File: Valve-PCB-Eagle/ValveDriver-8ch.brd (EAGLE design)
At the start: 101.6 x 63.5 mm, 21 parts, among them IC1 ULQ2803A, J10 Valve 3, J11 Valve 2, J12 Valve 1, J4 POWER_JACK, J5 Valve 8, J6 Valve 7, J7 Valve 6, J8 Valve 5, J9 Valve 4

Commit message: [Valve][Teensy] Fix mistaken labeling of Lick1/Lick2 pins
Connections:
- net LICK_1: now also J14.2, U$1.8; no longer J14.3, U$1.7
- net LICK_2: now also J14.3, U$1.7; no longer J14.2, U$1.8
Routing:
- net LICK_2: track 73.5 -> 84.7 mm
- net LICK_1: track 84.7 -> 73.5 mm
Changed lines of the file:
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@@
 <wire x1="56.53" y1="52.07" x2="29.21" y2="52.07" width="0.3048" layer="1"/>
 </signal>
-<signal name="LICK_1">
+<signal name="LICK_2">
 <contactref element="U$1" pad="7"/>
 <contactref element="J14" pad="3"/>
@@
 <wire x1="29.21" y1="26.67" x2="95.25" y2="26.67" width="0.3048" layer="1"/>
 </signal>
-<signal name="LICK_2">
+<signal name="LICK_1">
 <contactref element="U$1" pad="8"/>
 <contactref element="J14" pad="2"/>

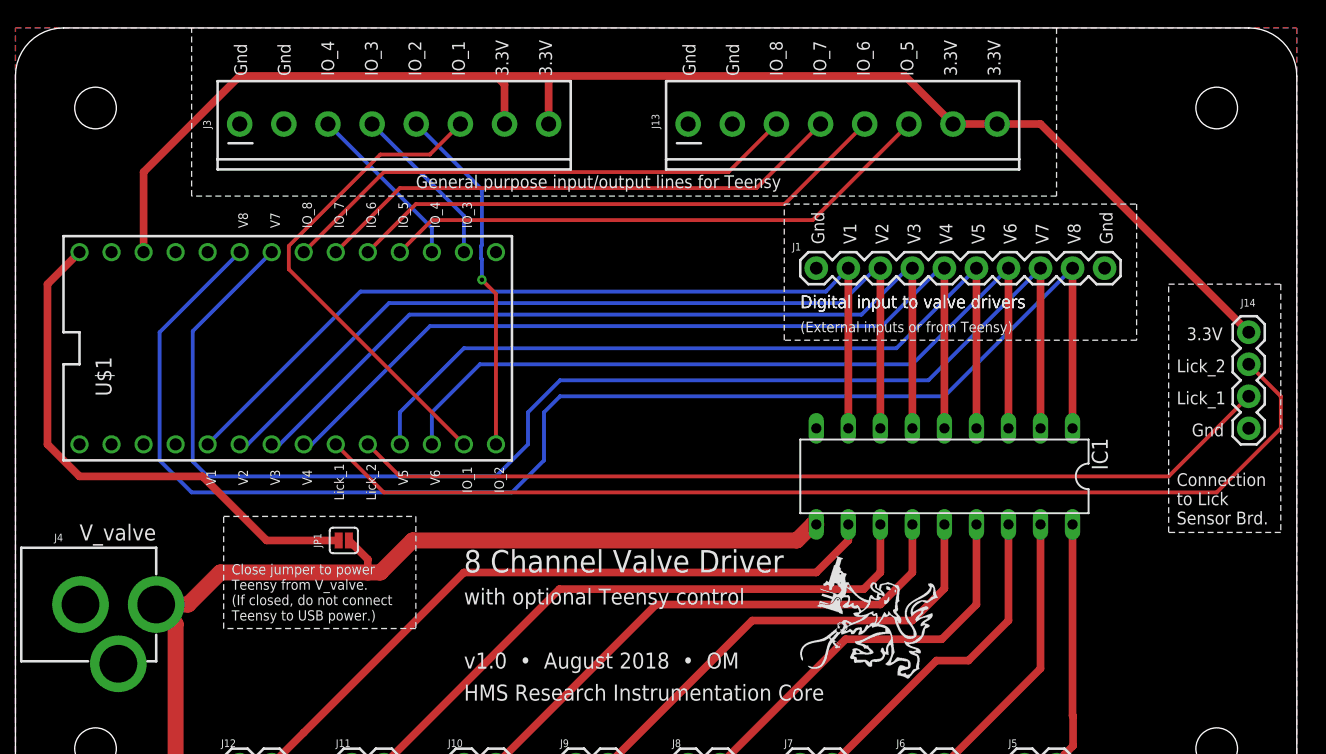
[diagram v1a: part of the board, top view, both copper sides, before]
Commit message: [Valve] Add 5V to screw term (fixes #6)
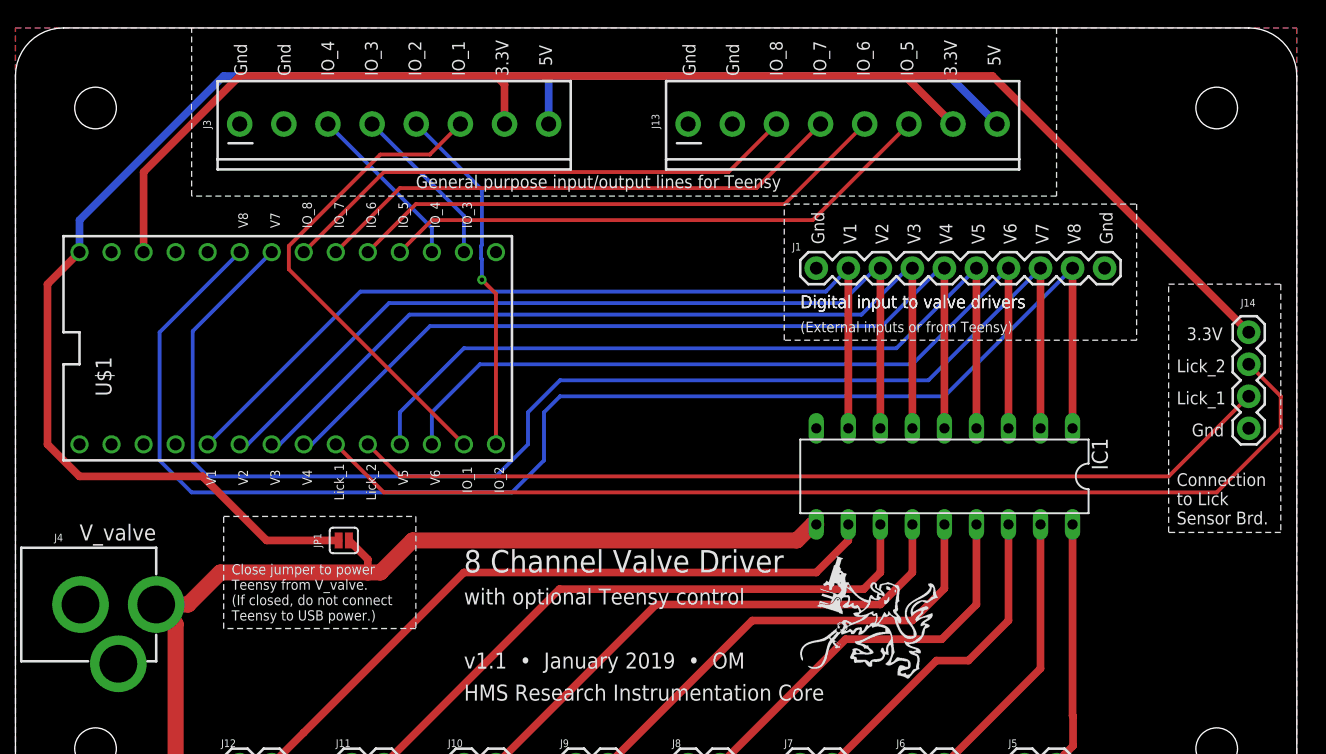
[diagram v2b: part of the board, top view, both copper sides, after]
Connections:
- net 3.3V: no longer J13.8, J3.8
- net V_IN_TEENSY: now also J13.8, J3.8
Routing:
- net V_IN_TEENSY: track 42.5 -> 128.1 mm
- net 3.3V: track 113.6 -> 115.0 mm
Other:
- board text added: "Gnd Gnd IO_4 IO_3 IO_2 IO_1 3.3V 5V"
- board text added: "Gnd Gnd IO_8 IO_7 IO_6 IO_5 3.3V 5V"
- board text added: "v1.1 • January 2019 • OM"
- board text removed: "Gnd Gnd IO_4 IO_3 IO_2 IO_1 3.3V 3.3V"
- board text removed: "Gnd Gnd IO_8 IO_7 IO_6 IO_5 3.3V 3.3V"
- board text removed: "v1.0 • August 2018 • OM"
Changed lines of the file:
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@@
 <?xml version="1.0" encoding="utf-8"?>
 <!DOCTYPE eagle SYSTEM "eagle.dtd">
-<eagle version="9.1.1">
+<eagle version="9.2.2">
 <drawing>
 <settings>
@@
 <setting verticaltext="up"/>
 </settings>
-<grid distance="0.1" unitdist="inch" unit="inch" style="dots" multiple="1" display="yes" altdistance="0.025" altunitdist="inch" altunit="inch"/>
+<grid distance="0.05" unitdist="inch" unit="inch" style="lines" multiple="2" display="yes" altdistance="0.025" altunitdist="inch" altunit="inch"/>
 <layers>
 <layer number="1" name="Top" color="4" fill="1" visible="yes" active="yes"/>
@@
 <layer number="18" name="Vias" color="2" fill="1" visible="yes" active="yes"/>
 <layer number="19" name="Unrouted" color="6" fill="1" visible="yes" active="yes"/>
-<layer number="20" name="Dimension" color="24" fill="1" visible="yes" active="yes"/>
-<layer number="21" name="tPlace" color="7" fill="1" visible="yes" active="yes"/>
-<layer number="22" name="bPlace" color="7" fill="1" visible="yes" active="yes"/>
-<layer number="23" name="tOrigins" color="15" fill="1" visible="no" active="yes"/>
-<layer number="24" name="bOrigins" color="15" fill="1" visible="no" active="yes"/>
-<layer number="25" name="tNames" color="7" fill="1" visible="yes" active="yes"/>
-<layer number="26" name="bNames" color="7" fill="1" visible="yes" active="yes"/>
-<layer number="27" name="tValues" color="7" fill="1" visible="yes" active="yes"/>
-<layer number="28" name="bValues" color="7" fill="1" visible="yes" active="yes"/>
+<layer number="20" name="Dimension" color="15" fill="1" visible="yes" active="yes"/>
+<layer number="21" name="tPlace" color="15" fill="1" visible="yes" active="yes"/>
+<layer number="22" name="bPlace" color="14" fill="1" visible="yes" active="yes"/>
+<layer number="23" name="tOrigins" color="15" fill="1" visible="yes" active="yes"/>
+<layer number="24" name="bOrigins" color="15" fill="1" visible="yes" active="yes"/>
+<layer number="25" name="tNames" color="15" fill="1" visible="no" active="yes"/>
+<layer number="26" name="bNames" color="15" fill="1" visible="no" active="yes"/>
+<layer number="27" name="tValues" color="7" fill="1" visible="no" active="yes"/>
+<layer number="28" name="bValues" color="7" fill="1" visible="no" active="yes"/>
 <layer number="29" name="tStop" color="7" fill="3" visible="no" active="yes"/>
 <layer number="30" name="bStop" color="7" fill="6" visible="no" active="yes"/>
@@
 <layer number="37" name="tTest" color="7" fill="1" visible="no" active="yes"/>
 <layer number="38" name="bTest" color="7" fill="1" visible="no" active="yes"/>
-<layer number="39" name="tKeepout" color="4" fill="11" visible="yes" active="yes"/>
-<layer number="40" name="bKeepout" color="1" fill="11" visible="yes" active="yes"/>
-<layer number="41" name="tRestrict" color="4" fill="10" visible="yes" active="yes"/>
-<layer number="42" name="bRestrict" color="1" fill="10" visible="yes" active="yes"/>
+<layer number="39" name="tKeepout" color="4" fill="11" visible="no" active="yes"/>
+<layer number="40" name="bKeepout" color="1" fill="11" visible="no" active="yes"/>
+<layer number="41" name="tRestrict" color="4" fill="10" visible="no" active="yes"/>
+<layer number="42" name="bRestrict" color="1" fill="10" visible="no" active="yes"/>
 <layer number="43" name="vRestrict" color="2" fill="10" visible="no" active="yes"/>
 <layer number="44" name="Drills" color="7" fill="1" visible="no" active="yes"/>
-<layer number="45" name="Holes" color="7" fill="1" visible="no" active="yes"/>
+<layer number="45" name="Holes" color="7" fill="1" visible="yes" active="yes"/>
 <layer number="46" name="Milling" color="3" fill="1" visible="no" active="yes"/>
 <layer number="47" name="Measures" color="7" fill="1" visible="no" active="yes"/>
@@
 <layer number="49" name="Reference" color="7" fill="1" visible="no" active="yes"/>
 <layer number="50" name="dxf" color="7" fill="1" visible="no" active="no"/>
-<layer number="51" name="tDocu" color="7" fill="1" visible="yes" active="yes"/>
-<layer number="52" name="bDocu" color="7" fill="1" visible="yes" active="yes"/>
+<layer number="51" name="tDocu" color="6" fill="1" visible="yes" active="yes"/>
+<layer number="52" name="bDocu" color="7" fill="1" visible="no" active="yes"/>
 <layer number="53" name="tGND_GNDA" color="7" fill="9" visible="no" active="no"/>
 <layer number="54" name="bGND_GNDA" color="1" fill="9" visible="no" active="no"/>
@@
 <text x="35.56" y="20.32" size="1.778" layer="21" ratio="15">8 Channel Valve Driver</text>
 <text x="35.56" y="17.78" size="1.27" layer="21" ratio="15">with optional Teensy control</text>
-<text x="35.56" y="12.7" size="1.27" layer="21" ratio="10">v1.0  •  August 2018  •  OM</text>
+<text x="35.56" y="12.7" size="1.27" layer="21" ratio="10">v1.1  •  January 2019  •  OM</text>
 <text x="35.56" y="10.16" size="1.27" layer="21" ratio="10">HMS Research Instrumentation Core</text>
 <text x="17.145" y="16.51" size="0.8128" layer="21" ratio="12">Close jumper to power
@@
 IO_1
 3.3V
-3.3V</text>
+  5V</text>
 <text x="78.105" y="59.69" size="1.016" layer="21" ratio="15" distance="240" rot="R90">Gnd
 Gnd
@@
 IO_5
 3.3V
-3.3V</text>
+  5V</text>
 <text x="31.75" y="50.8" size="1.016" layer="21">General purpose input/output lines for Teensy</text>
 <wire x1="13.97" y1="50.165" x2="13.97" y2="63.5" width="0.0762" layer="21" style="shortdash"/>
@@
 </autorouter>
 <elements>
-<element name="IC1" library="uln-udn" library_urn="urn:adsk.eagle:library:407" package="DIL18" package3d_urn="urn:adsk.eagle:package:30237/1" value="ULQ2803A" x="73.66" y="27.94" rot="R180"/>
+<element name="IC1" library="uln-udn" library_urn="urn:adsk.eagle:library:407" package="DIL18" package3d_urn="urn:adsk.eagle:package:30237/1" value="ULQ2803A" x="73.66" y="27.94" smashed="yes" rot="R180">
+<attribute name="NAME" x="85.344" y="30.988" size="1.27" layer="25" ratio="10" rot="R270"/>
+<attribute name="VALUE" x="83.185" y="28.575" size="1.27" layer="27" ratio="10" rot="R180"/>
+</element>
 <element name="J1" library="SparkFun-Connectors" package="1X10" value="" x="63.5" y="44.45" smashed="yes">
 <attribute name="NAME" x="61.595" y="45.847" size="0.6096" layer="25" font="vector" ratio="15"/>
@@
 <attribute name="NAME" x="24.257" y="22.86" size="0.6096" layer="25" font="vector" ratio="15" rot="R90" align="bottom-center"/>
 </element>
-<element name="U$3" library="ofer-eagle-lib" package="RIC_LOGO_MED" value="" x="62.23" y="11.8872"/>
+<element name="U$3" library="ofer-eagle-lib" package="RIC_LOGO_MED" value="" x="62.23" y="11.8872" smashed="yes"/>
 <element name="U$2" library="SparkFun-Hardware" library_urn="urn:adsk.eagle:library:519" package="STAND-OFF" package3d_urn="urn:adsk.eagle:package:38630/1" value="" x="95.25" y="57.15" smashed="yes">
 <attribute name="VALUE" x="95.25" y="55.118" size="0.6096" layer="27" font="vector" ratio="20" align="top-center"/>
@@
 <wire x1="10.16" y1="52.07" x2="17.78" y2="59.69" width="0.6096" layer="1"/>
 <wire x1="17.78" y1="59.69" x2="38.1" y2="59.69" width="0.6096" layer="1"/>
-<wire x1="38.1" y1="59.69" x2="41.91" y2="59.69" width="0.6096" layer="1"/>
-<wire x1="41.91" y1="59.69" x2="70.53" y2="59.69" width="0.6096" layer="1"/>
+<wire x1="38.1" y1="59.69" x2="70.53" y2="59.69" width="0.6096" layer="1"/>
 <wire x1="70.53" y1="59.69" x2="74.34" y2="55.88" width="0.6096" layer="1"/>
 <wire x1="38.78" y1="55.88" x2="38.78" y2="59.01" width="0.6096" layer="1"/>
 <wire x1="38.78" y1="59.01" x2="38.1" y2="59.69" width="0.6096" layer="1"/>
-<contactref element="J13" pad="8"/>
-<contactref element="J3" pad="8"/>
 <contactref element="J14" pad="4"/>
-<wire x1="42.28" y1="55.88" x2="42.28" y2="59.32" width="0.6096" layer="1"/>
-<wire x1="42.28" y1="59.32" x2="41.91" y2="59.69" width="0.6096" layer="1"/>
-<wire x1="74.34" y1="55.88" x2="77.84" y2="55.88" width="0.6096" layer="1"/>
-<wire x1="77.84" y1="55.88" x2="81.28" y2="55.88" width="0.6096" layer="1"/>
-<wire x1="81.28" y1="55.88" x2="97.79" y2="39.37" width="0.6096" layer="1"/>
+<wire x1="70.53" y1="59.69" x2="77.47" y2="59.69" width="0.6096" layer="1"/>
+<wire x1="77.47" y1="59.69" x2="97.79" y2="39.37" width="0.6096" layer="1"/>
 </signal>
 <signal name="GND" class="1">
@@
 <wire x1="19.9136" y1="22.86" x2="25.6286" y2="22.86" width="0.6096" layer="1"/>
 <wire x1="5.08" y1="27.94" x2="14.8336" y2="27.94" width="0.6096" layer="1"/>
+<contactref element="J3" pad="8"/>
+<contactref element="J13" pad="8"/>
+<wire x1="5.08" y1="45.72" x2="5.08" y2="48.26" width="0.6096" layer="16"/>
+<wire x1="5.08" y1="48.26" x2="16.51" y2="59.69" width="0.6096" layer="16"/>
+<wire x1="16.51" y1="59.69" x2="41.91" y2="59.69" width="0.6096" layer="16"/>
+<wire x1="41.91" y1="59.69" x2="42.28" y2="59.32" width="0.6096" layer="16"/>
+<wire x1="42.28" y1="59.32" x2="42.28" y2="55.88" width="0.6096" layer="16"/>
+<wire x1="41.91" y1="59.69" x2="74.03" y2="59.69" width="0.6096" layer="16"/>
+<wire x1="74.03" y1="59.69" x2="77.84" y2="55.88" width="0.6096" layer="16"/>
 </signal>
 </signals>

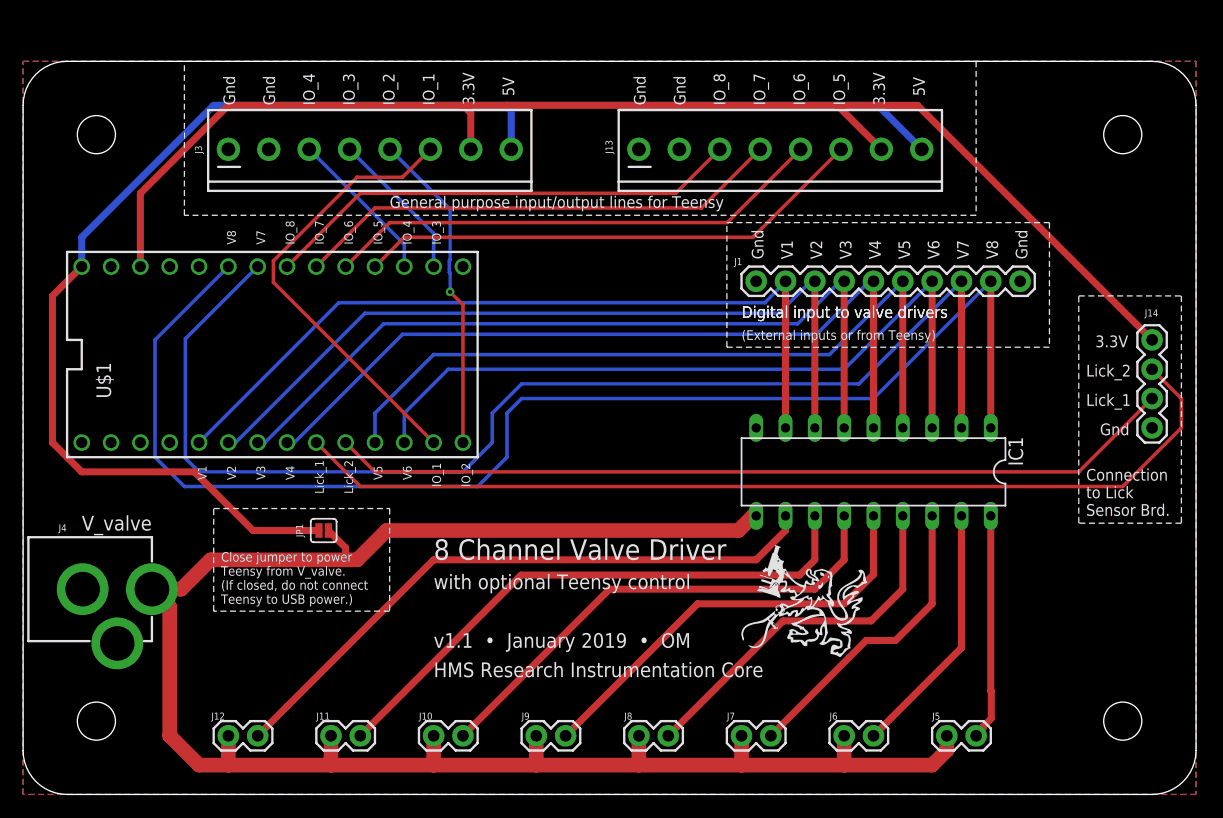
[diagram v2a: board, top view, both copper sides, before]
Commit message: [Valve] Make minor tweaks to board size & layout
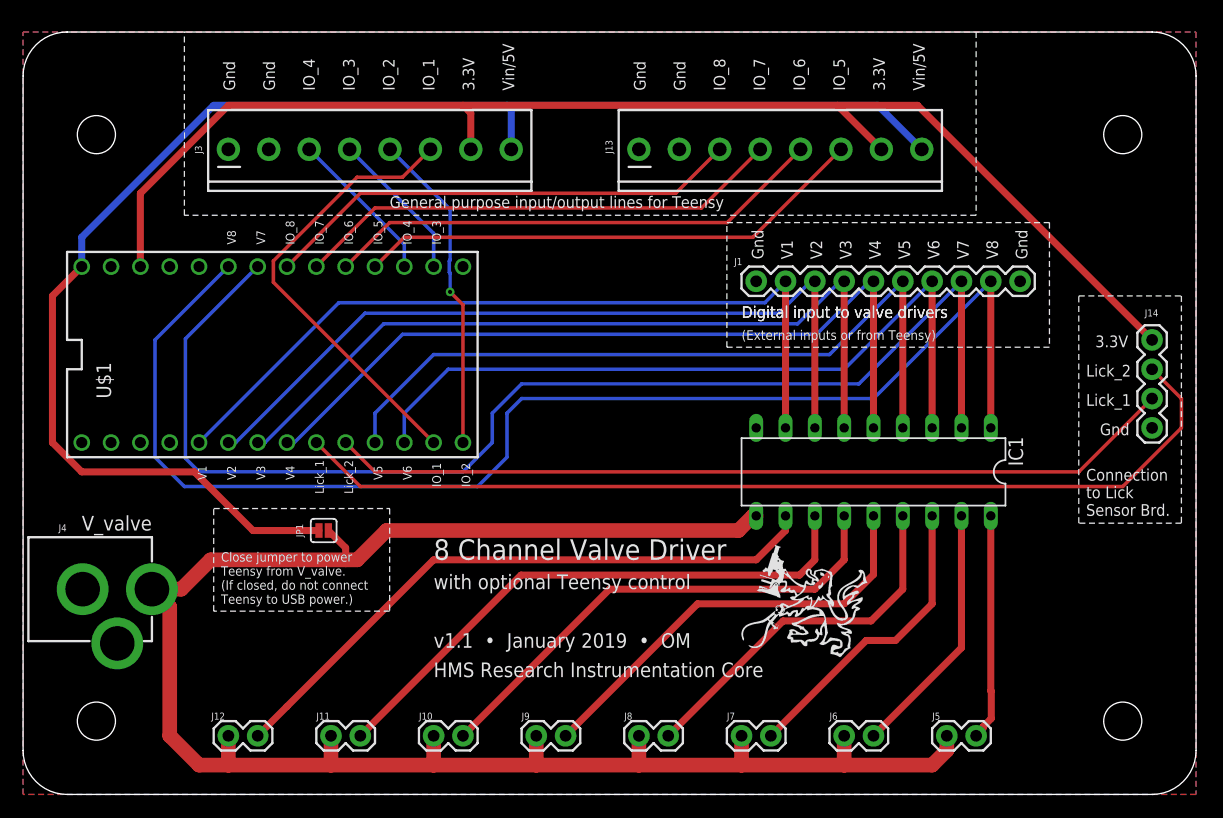
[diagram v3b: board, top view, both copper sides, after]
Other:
- board size 101.6 x 63.5 mm -> 101.6 x 66 mm
- board text added: "Gnd Gnd IO_4 IO_3 IO_2 IO_1 3.3V Vin/5V"
- board text added: "Gnd Gnd IO_8 IO_7 IO_6 IO_5 3.3V Vin/5V"
- board text removed: "Gnd Gnd IO_4 IO_3 IO_2 IO_1 3.3V 5V"
- board text removed: "Gnd Gnd IO_8 IO_7 IO_6 IO_5 3.3V 5V"
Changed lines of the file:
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@@
 <board>
 <plain>
-<wire x1="0" y1="59.69" x2="0" y2="3.81" width="0" layer="20"/>
+<wire x1="0" y1="62.23" x2="0" y2="3.81" width="0" layer="20"/>
 <wire x1="0" y1="3.81" x2="3.81" y2="0" width="0" layer="20" curve="90"/>
 <wire x1="3.81" y1="0" x2="97.79" y2="0" width="0" layer="20"/>
 <wire x1="97.79" y1="0" x2="101.6" y2="3.81" width="0" layer="20" curve="90"/>
-<wire x1="101.6" y1="3.81" x2="101.6" y2="59.69" width="0" layer="20"/>
-<wire x1="101.6" y1="59.69" x2="97.79" y2="63.5" width="0" layer="20" curve="90"/>
-<wire x1="97.79" y1="63.5" x2="3.81" y2="63.5" width="0" layer="20"/>
-<wire x1="3.81" y1="63.5" x2="0" y2="59.69" width="0" layer="20" curve="90"/>
+<wire x1="101.6" y1="3.81" x2="101.6" y2="62.23" width="0" layer="20"/>
+<wire x1="101.6" y1="62.23" x2="97.79" y2="66.04" width="0" layer="20" curve="90"/>
+<wire x1="97.79" y1="66.04" x2="3.81" y2="66.04" width="0" layer="20"/>
+<wire x1="3.81" y1="66.04" x2="0" y2="62.23" width="0" layer="20" curve="90"/>
 <text x="35.56" y="20.32" size="1.778" layer="21" ratio="15">8 Channel Valve Driver</text>
 <text x="35.56" y="17.78" size="1.27" layer="21" ratio="15">with optional Teensy control</text>
@@
 <text x="62.23" y="41.275" size="1.016" layer="21">Digital input to valve drivers</text>
 <text x="62.23" y="39.37" size="0.8382" layer="21" ratio="10">(External inputs or from Teensy)</text>
-<text x="42.545" y="59.69" size="1.016" layer="21" ratio="15" distance="240" rot="R90">Gnd
+<text x="42.545" y="60.96" size="1.016" layer="21" ratio="15" distance="240" rot="R90">Gnd
 Gnd
 IO_4
@@
 IO_1
 3.3V
-  5V</text>
-<text x="78.105" y="59.69" size="1.016" layer="21" ratio="15" distance="240" rot="R90">Gnd
+Vin/5V</text>
+<text x="78.105" y="60.96" size="1.016" layer="21" ratio="15" distance="240" rot="R90">Gnd
 Gnd
 IO_8
@@
 IO_5
 3.3V
-  5V</text>
+Vin/5V</text>
 <text x="31.75" y="50.8" size="1.016" layer="21">General purpose input/output lines for Teensy</text>
-<wire x1="13.97" y1="50.165" x2="13.97" y2="63.5" width="0.0762" layer="21" style="shortdash"/>
-<wire x1="82.55" y1="63.5" x2="82.55" y2="50.165" width="0.0762" layer="21" style="shortdash"/>
+<wire x1="13.97" y1="50.165" x2="13.97" y2="66.04" width="0.0762" layer="21" style="shortdash"/>
+<wire x1="82.55" y1="66.04" x2="82.55" y2="50.165" width="0.0762" layer="21" style="shortdash"/>
 <wire x1="82.55" y1="50.165" x2="13.97" y2="50.165" width="0.0762" layer="21" style="shortdash"/>
 <text x="5.08" y="22.86" size="1.27" layer="21" ratio="10">V_valve</text>
@@
 <contactref element="J4" pad="GNDBREAK"/>
 <polygon width="0.1524" layer="16">
-<vertex x="0" y="63.5"/>
-<vertex x="101.6" y="63.5"/>
+<vertex x="0" y="66.04"/>
+<vertex x="101.6" y="66.04"/>
 <vertex x="101.6" y="0"/>
 <vertex x="0" y="0"/>
@@
 <contactref element="J13" pad="2"/>
 <polygon width="0.1524" layer="1">
-<vertex x="0" y="63.5"/>
-<vertex x="101.6" y="63.5"/>
+<vertex x="0" y="66.04"/>
+<vertex x="101.6" y="66.04"/>
 <vertex x="101.6" y="0"/>
 <vertex x="0" y="0"/>
